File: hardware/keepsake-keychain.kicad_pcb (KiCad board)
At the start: 2 copper layers, 80 x 30 mm, 95 parts, among them Q1 MMFTP4042K, Q2 MMFTP4042K, Q3 MMFTP4042K, Q4 MMFTP4042K, SW1 SPDT Power Switch, SW2 PTS636 SK25J SMTR LFS, U1 74HC595, U2 74HC595, U3 74HC595, U4 Op Amp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

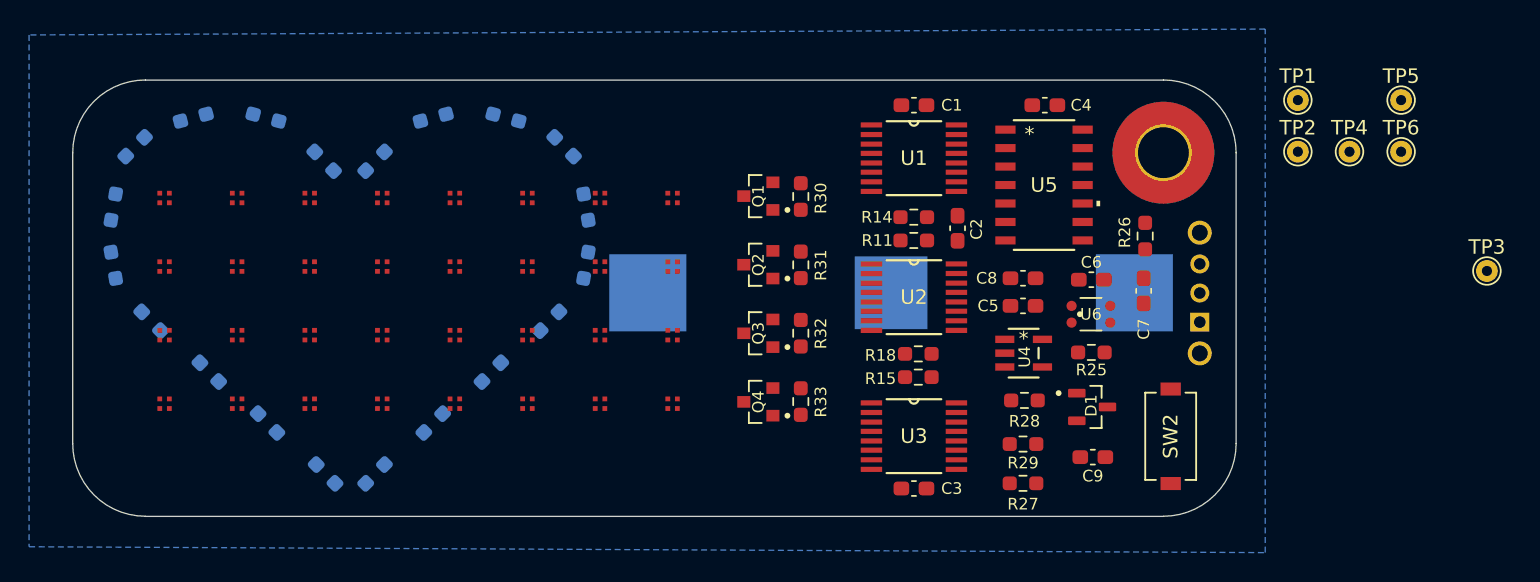
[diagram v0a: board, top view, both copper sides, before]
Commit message: Replace tactile push button for stable, lower profile
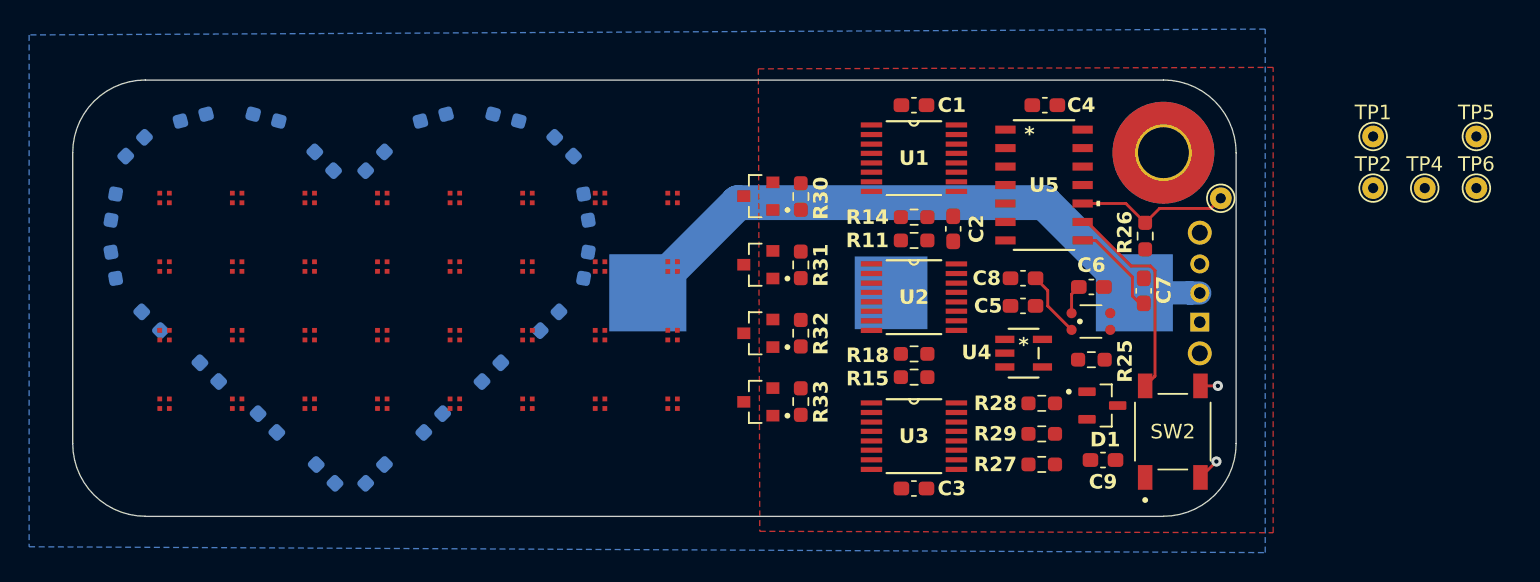
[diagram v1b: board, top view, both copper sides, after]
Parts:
- SW2: footprint 0_Tactile_Push_Button:SW_PTS636_SM43J_SMTR_LFS -> 0_Tactile_Push_Button:SW_TS18-5-15-SL-160-SMT-TR
- moved TP3 19.0 mm to (188.8, 87.6)
- moved TP1 5.75 mm to (199.3, 83.3)
- moved TP2 5.75 mm to (199.3, 86.9)
- moved TP5 5.75 mm to (206.4, 83.3)
- moved TP6 5.75 mm to (206.4, 86.9)
- moved TP4 5.75 mm to (202.8, 86.9)
- moved R27 1.83 mm to (176.5, 105.9)
- moved R29 1.47 mm to (176.5, 103.8)
- moved R28 1.20 mm to (176.5, 101.7)
- moved C9 0.73 mm to (180.7, 105.6)
- moved D1 0.71 mm to (180.7, 101.8)
- moved C6 0.50 mm to (179.9, 93.7)
- moved R25 0.50 mm to (179.9, 98.7)
- moved U6 0.50 mm to (179.9, 96.0)
- moved SW2 0.35 mm to (185.5, 103.6), turned to 90 degrees
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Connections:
- SW2 pad 2: GND -> Net-(U5-PB0)
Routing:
- net Net-(BT1-Pad1): track 0.00 -> 43.1 mm
- net Net-(U5-PB0): track 0.00 -> 14.6 mm
- net Net-(U5-PA0/*RESET/UPDI): track 0.00 -> 10.7 mm
- net MIC: track 0.00 -> 6.75 mm
- net Net-(U6-OUTPUT): track 0.00 -> 4.58 mm
- net GND: track 0.00 -> 2.76 mm, vias 0 -> 2
- net +3V3: track 0.00 -> 2.01 mm
- added copper zone on F.Cu, net +3V3

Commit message: Route all traces for controller
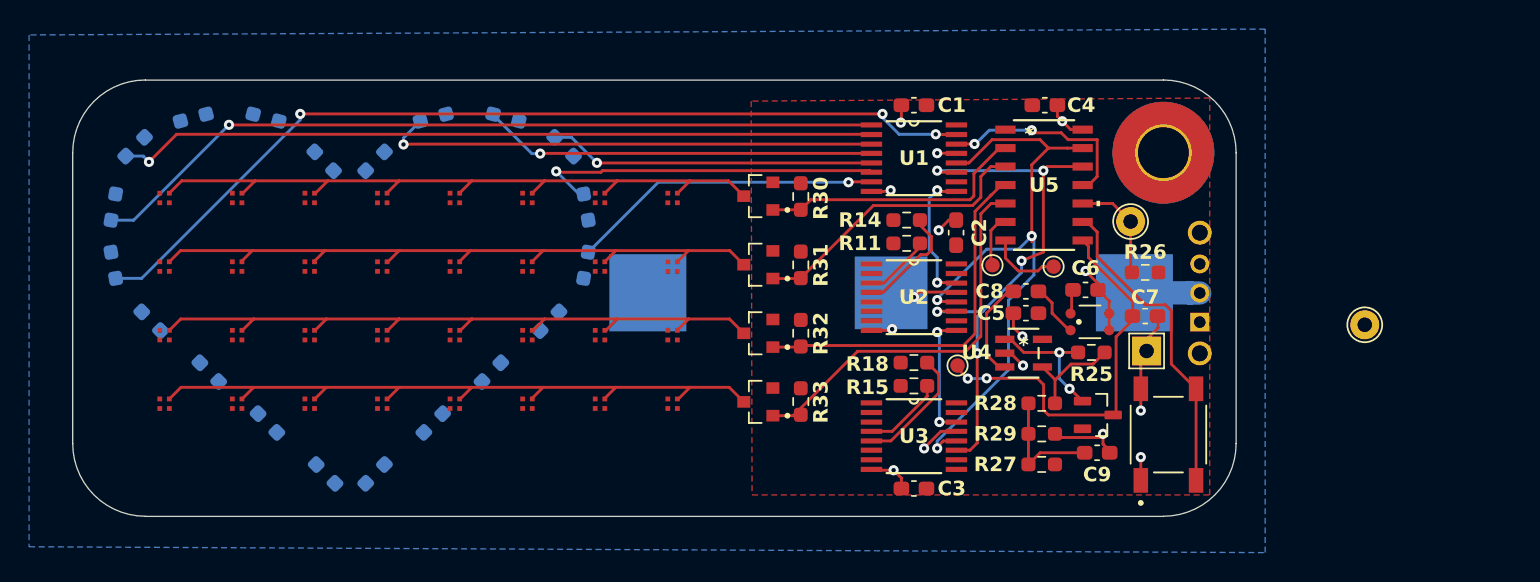
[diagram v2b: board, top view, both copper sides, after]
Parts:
- TP1, TP3: footprint TestPoint:TestPoint_THTPad_D1.5mm_Drill0.7mm -> TestPoint:TestPoint_THTPad_D2.0mm_Drill1.0mm
- TP2: footprint TestPoint:TestPoint_THTPad_D1.5mm_Drill0.7mm -> TestPoint:TestPoint_THTPad_2.0x2.0mm_Drill1.0mm
- TP4, TP5, TP6: footprint TestPoint:TestPoint_THTPad_D1.5mm_Drill0.7mm -> TestPoint:TestPoint_Pad_D1.0mm
- moved TP5 34.4 mm to (173.1, 92.2)
- moved TP4 34.4 mm to (170.7, 99.1)
- moved TP6 29.6 mm to (177.3, 92.3)
- moved TP2 19.2 mm to (183.7, 98.1)
- moved TP1 13.0 mm to (198.7, 96.3)
- moved TP3 6.40 mm to (182.6, 89.2)
- moved R26 2.50 mm to (183.6, 92.7), turned to 0 degrees
- moved C7 1.74 mm to (183.6, 95.7), turned to 180 degrees
- moved C8 0.92 mm to (175.4, 94.0)
- moved D1 0.72 mm to (180.3, 102.5)
- moved C9 0.64 mm to (180.3, 105.1)
- moved R15 0.60 mm to (167.7, 100.5)
- moved R18 0.60 mm to (167.7, 98.9)
- moved R11 0.55 mm to (167.2, 90.7)
- moved R14 0.55 mm to (167.2, 89.1)
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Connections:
- SW2 pad 1: Net-(U5-PB0) -> GND
- SW2 pad 2: Net-(U5-PB0) -> GND
- SW2 pad 3: GND -> Net-(U5-PB0)
- SW2 pad 4: GND -> Net-(U5-PB0)
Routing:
- net Net-(U1-Q0): track 0.00 -> 63.5 mm, vias 0 -> 3
- net Net-(U1-Q1): track 0.00 -> 55.2 mm, vias 0 -> 1
- net Net-(U1-Q2): track 0.00 -> 52.2 mm, vias 0 -> 1
- net ROW_0: track 0.00 -> 48.8 mm
- net ROW_3: track 0.00 -> 48.3 mm
- net ROW_2: track 0.00 -> 48.3 mm
- net ROW_1: track 0.00 -> 47.8 mm
- net LATCH_CLK: track 0.00 -> 45.7 mm, vias 0 -> 3
- net SHIFT_CLK: track 0.00 -> 38.9 mm, vias 0 -> 5
- net GND: track 2.76 -> 41.4 mm, vias 2 -> 15
- net Net-(BT1-Pad1): track 43.1 -> 4.50 mm
- net Net-(U1-Q3): track 0.00 -> 34.3 mm, vias 0 -> 1
- net S_ROW_3: track 0.00 -> 27.5 mm
- net Net-(U1-Q4): track 0.00 -> 27.2 mm, vias 0 -> 1
- net S_ROW_2: track 0.00 -> 25.6 mm
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
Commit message: Route first half of LED traces
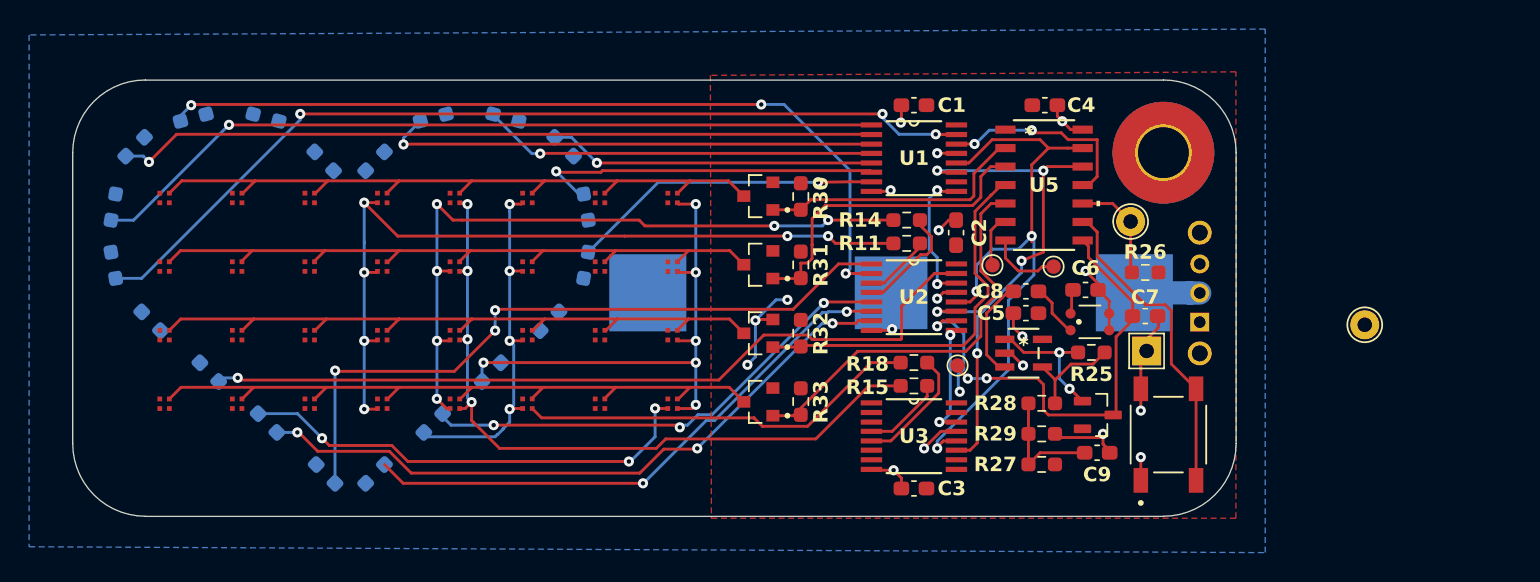
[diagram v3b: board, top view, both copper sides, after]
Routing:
- net Net-(U2-Q2): track 0.00 -> 57.6 mm, vias 0 -> 3
- net GREEN_3: track 0.00 -> 55.7 mm, vias 0 -> 6
- net Net-(U2-Q0): track 0.00 -> 55.6 mm, vias 0 -> 1
- net RED_4: track 0.00 -> 49.9 mm, vias 0 -> 4
- net GREEN_4: track 0.00 -> 48.6 mm, vias 0 -> 6
- net Net-(U2-Q1): track 0.00 -> 48.4 mm, vias 0 -> 3
- net Net-(U2-Q7): track 0.00 -> 46.4 mm, vias 0 -> 3
- net Net-(U2-Q6): track 0.00 -> 38.9 mm, vias 0 -> 2
- net RED_7: track 0.00 -> 35.0 mm, vias 0 -> 6
- net Net-(U2-Q5): track 0.00 -> 33.6 mm, vias 0 -> 3
- net GREEN_7: track 0.00 -> 32.2 mm, vias 0 -> 3
- net RED_5: track 0.00 -> 27.7 mm
- net GREEN_5: track 0.00 -> 25.3 mm, vias 0 -> 4
- net +3V3: track 1.64 -> 16.9 mm, vias 0 -> 5
- net S_ROW_1: track 20.0 -> 22.2 mm
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
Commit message: Convert to four-layer board (sigh)
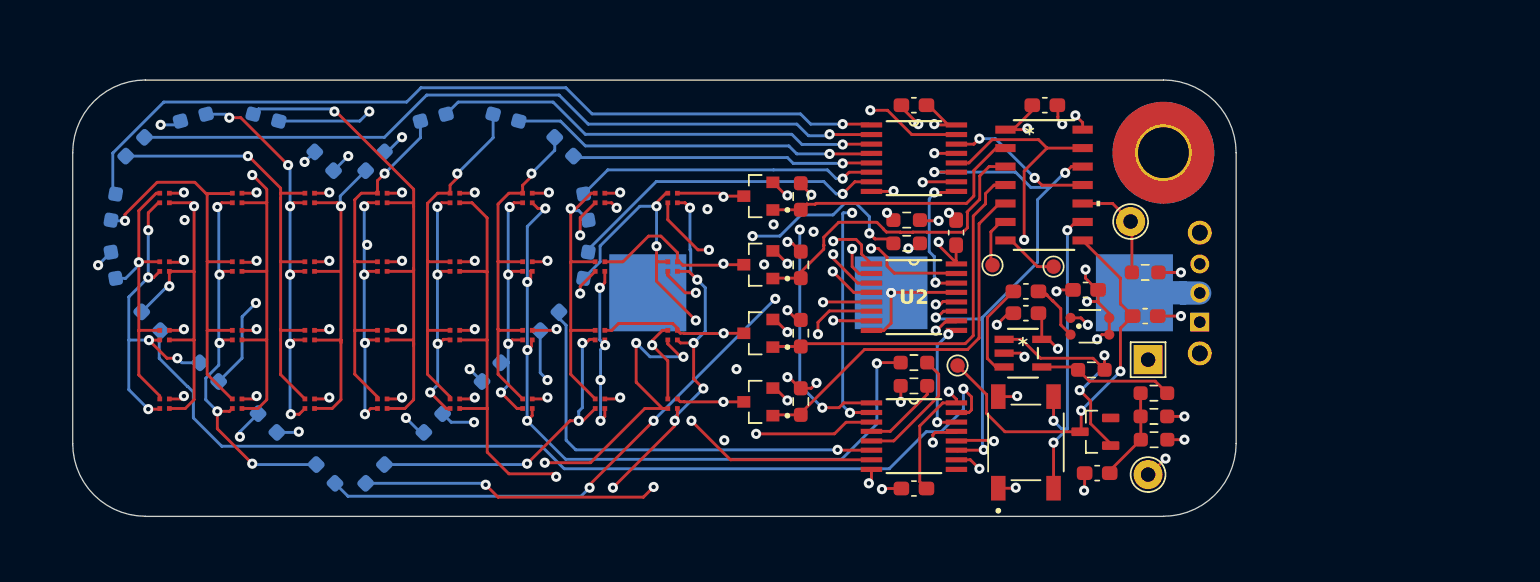
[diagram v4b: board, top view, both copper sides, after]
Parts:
- moved TP1 18.1 mm to (183.8, 106.6)
- moved SW2 9.81 mm to (175.4, 104.3)
- moved R27 7.91 mm to (184.2, 104.2)
- moved R29 7.81 mm to (184.2, 102.6)
- moved R28 7.74 mm to (184.2, 101.0)
- moved R17 5.32 mm to (138.6, 99.5), turned to -135 degrees
- moved R24 5.32 mm to (134.6, 103.0), turned to -135 degrees
- moved C9 1.40 mm to (180.3, 106.5), turned to 180 degrees
- moved R25 1.20 mm to (179.9, 99.4), turned to 180 degrees
- moved D1 1.17 mm to (180.2, 103.6), turned to 180 degrees
- moved TP2 0.61 mm to (183.8, 98.7)
- moved U6 0.30 mm to (179.8, 96.4)
- turned R1 to 100 degrees
- turned R10 to 15 degrees
- turned R12 to -15 degrees
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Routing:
- net Net-(U3-Q0): track 0.00 -> 67.3 mm, vias 0 -> 1
- net Net-(U3-Q3): track 0.00 -> 53.0 mm, vias 0 -> 2
- net Net-(U3-Q2): track 0.00 -> 51.8 mm, vias 0 -> 3
- net Net-(U3-Q1): track 0.00 -> 51.0 mm, vias 0 -> 3
- net RED_3: track 0.00 -> 35.9 mm, vias 0 -> 1
- net Net-(U3-Q7): track 0.00 -> 35.2 mm, vias 0 -> 2
- net GREEN_6: track 0.00 -> 34.6 mm, vias 0 -> 5
- net BLUE_2: track 0.00 -> 31.9 mm, vias 0 -> 1
- net +3V3: track 16.9 -> 48.4 mm, vias 5 -> 22
- net Net-(U3-Q6): track 0.00 -> 30.4 mm, vias 0 -> 1
- net GREEN_7: track 32.2 -> 61.3 mm, vias 3 -> 6
- net GREEN_2: track 0.00 -> 28.8 mm, vias 0 -> 6
- net BLUE_1: track 0.00 -> 28.4 mm, vias 0 -> 1
- net GREEN_1: track 0.00 -> 28.3 mm, vias 0 -> 5
- net BLUE_7: track 0.00 -> 28.1 mm, vias 0 -> 4
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- added copper zone on In2.Cu, net +3V3
- added copper zone on In1.Cu, net GND
- removed copper zone on F.Cu, net +3V3
- removed copper zone on B.Cu, net GND
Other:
- copper layers 2 -> 4
- board text added: "Est. Aug 15 2026"
- board text added: "Sixteen years and we never changed our minds"
- board text added: "Stephie & Eric McDaniel"

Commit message: Clean BOM, export gerbers
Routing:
- net GND: track 37.8 -> 32.7 mm, vias 20 -> 21
- net MIC: track 27.1 -> 27.7 mm
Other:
- board text added: "Est. Aug 15, 2026"
- board text removed: "Est. Aug 15 2026"

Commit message: Tweak layout for additional GND pour
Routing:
- net Net-(U1-Q7): track 22.2 -> 25.0 mm
- net Net-(U1-Q7_2): track 9.52 -> 11.7 mm
- net Net-(U3-Q2): track 51.8 -> 53.6 mm
- net BLUE_7: track 28.1 -> 26.7 mm
- net Net-(U1-Q1): track 58.1 -> 59.4 mm, vias 1 -> 3
- net S_ROW_2: track 26.0 -> 27.0 mm
- net RED_5: track 51.0 -> 51.9 mm
- net Net-(U1-Q2): track 52.4 -> 53.3 mm
- net S_ROW_3: track 27.1 -> 27.9 mm
- net Net-(U1-Q4): track 25.2 -> 25.9 mm
- added copper zone on B.Cu, net GND
